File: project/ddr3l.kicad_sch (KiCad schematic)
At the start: 0 parts

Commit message: Added CubeMX project and some schematic components are added
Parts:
- added C100, C101, C102, C88, C89, C90, C91, C94, C95, C96, C97, C98, C99: 100n, bozi:GRM15_T05, symbol Device:C
- added C92, C93: 10u, bozi:GRT18_T15, symbol Device:C
- added IC9: MT41K128M16JT-107_K, bozi:BGA96C80P9X16_800X1400X120_edit, symbol bozi:MT41K128M16JT-107_K
- added R16, R17: 10K, bozi:RESC1005X37N_edit, symbol Device:R
- added R18: 100, bozi:RESC1005X37N_edit, symbol Device:R
- added R19: 240, bozi:RESC1005X37N_edit, symbol Device:R
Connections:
- new net: IC9.L8 (ZQ), R19.2
- new net DDR_A0: IC9.N3 (A0)
- new net DDR_A1: IC9.P7 (A1)
- new net DDR_A10: IC9.L7 (A10/AP)
- new net DDR_A11: IC9.R7 (A11)
- new net DDR_A12: IC9.N7 (A12/BC#)
- new net DDR_A13: IC9.T3 (A13)
- new net DDR_A2: IC9.P3 (A2)
- new net DDR_A3: IC9.N2 (A3)
- new net DDR_A4: IC9.P8 (A4)
- new net DDR_A5: IC9.P2 (A5)
- new net DDR_A6: IC9.R8 (A6)
- new net DDR_A7: IC9.R2 (A7)
- new net DDR_A8: IC9.T8 (A8)
- new net DDR_A9: IC9.R3 (A9)
- new net DDR_BA0: IC9.M2 (BA0)
- new net DDR_BA1: IC9.N8 (BA1)
- new net DDR_BA2: IC9.M3 (BA2)
- new net DDR_CKE: IC9.K9 (CKE), R17.1
- new net DDR_CLKN: IC9.K7 (CK#), R18.2
- new net DDR_CLKP: IC9.J7 (CK), R18.1
- new net DDR_DQ0: IC9.A7 (DQ12)
- new net DDR_DQ1: IC9.B8 (DQ14)
- new net DDR_DQ10: IC9.G2 (DQ6)
- new net DDR_DQ11: IC9.H8 (DQ5)
- new net DDR_DQ12: IC9.F8 (DQ3)
- new net DDR_DQ13: IC9.F2 (DQ2)
- new net DDR_DQ14: IC9.H7 (DQ7)
- new net DDR_DQ15: IC9.F7 (DQ1)
- new net DDR_DQ2: IC9.D7 (DQ8)
- new net DDR_DQ3: IC9.A3 (DQ15)
- new net DDR_DQ4: IC9.C8 (DQ10)
- new net DDR_DQ5: IC9.A2 (DQ13)
- new net DDR_DQ6: IC9.C2 (DQ11)
- new net DDR_DQ7: IC9.C3 (DQ9)
- new net DDR_DQ8: IC9.E3 (DQ0)
- new net DDR_DQ9: IC9.H3 (DQ4)
- new net DDR_DQM0: IC9.D3 (UDM)
- new net DDR_DQM1: IC9.E7 (LDM)
- new net DDR_DQS0N: IC9.B7 (UDQS#)
- new net DDR_DQS0P: IC9.C7 (UDQS)
- new net DDR_DQS1N: IC9.G3 (LDQS#)
- new net DDR_DQS1P: IC9.F3 (LDQS)
- new net DDR_ODT: IC9.K1 (ODT)
- new net GNDREF: C100.2, C101.2, C102.2, C88.2, C89.2, C90.2, C91.2, C92.2, C93.2, C94.2, C95.2, C96.2, C97.2, C98.2, C99.2, IC9.A9 (VSS_1), IC9.B1 (VSSQ_1), IC9.B3 (VSS_2), IC9.B9 (VSSQ_2), IC9.D1 (VSSQ_3), IC9.D8 (VSSQ_4), IC9.E1 (VSS_3), IC9.E2 (VSSQ_5), IC9.E8 (VSSQ_6), IC9.F9 (VSSQ_7), IC9.G1 (VSSQ_8), IC9.G8 (VSS_4), IC9.G9 (VSSQ_9), IC9.J2 (VSS_5), IC9.J8 (VSS_6), IC9.M1 (VSS_7), IC9.M9 (VSS_8), IC9.P1 (VSS_9), IC9.P9 (VSS_10), IC9.T1 (VSS_11), IC9.T9 (VSS_12), R16.2, R17.2, R19.1
- new net VDD_DDR: C100.1, C88.1, C89.1, C90.1, C91.1, C92.1, C93.1, C94.1, C95.1, C96.1, C97.1, C98.1, C99.1, IC9.A1 (VDDQ_1), IC9.A8 (VDDQ_2), IC9.B2 (VDD_1), IC9.C1 (VDDQ_3), IC9.C9 (VDDQ_4), IC9.D2 (VDDQ_5), IC9.D9 (VDD_2), IC9.E9 (VDDQ_6), IC9.F1 (VDDQ_7), IC9.G7 (VDD_3), IC9.H2 (VDDQ_8), IC9.H9 (VDDQ_9), IC9.K2 (VDD_4), IC9.K8 (VDD_5), IC9.N1 (VDD_6), IC9.N9 (VDD_7), IC9.R1 (VDD_8), IC9.R9 (VDD_9)
- new net VREF_DDR: C101.1, C102.1, IC9.H1 (VREFDQ), IC9.M8 (VREFCA)
- new net ~{DDR_CAS}: IC9.K3 (CAS#)
- new net ~{DDR_CS}: IC9.L2 (CS#)
- new net ~{DDR_RAS}: IC9.J3 (RAS#)
- new net ~{DDR_RESET}: IC9.T2 (RESET#), R16.1
- new net ~{DDR_WE}: IC9.L3 (WE#)
- no-connect marks 0 -> 5
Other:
- note added: "Connect to ground plane"

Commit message: schemtic is done, need to go through BOM
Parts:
- C100: renamed from C97; value 100n -> 100nF; Manufacturer_Name (none) -> Murata Electronics
- C101: renamed from C98; value 100n -> 100nF; Manufacturer_Name (none) -> Murata Electronics
- C102: renamed from C99; value 100n -> 100nF; Manufacturer_Name (none) -> Murata Electronics
- C103: renamed from C100; value 100n -> 100nF; Manufacturer_Name (none) -> Murata Electronics
- C104: renamed from C101; value 100n -> 100nF; Manufacturer_Name (none) -> Murata Electronics
- C105: renamed from C102; value 100n -> 100nF; Manufacturer_Name (none) -> Murata Electronics
- C91: renamed from C88; value 100n -> 100nF; Manufacturer_Name (none) -> Murata Electronics
- C92: renamed from C89; value 100n -> 100nF; Manufacturer_Name (none) -> Murata Electronics
- C93: renamed from C90; value 100n -> 100nF; Manufacturer_Name (none) -> Murata Electronics
- C94: renamed from C91; value 100n -> 100nF; Manufacturer_Name (none) -> Murata Electronics
- C95: renamed from C92; value 10u -> 10uF; Manufacturer_Name (none) -> Murata Electronics
- C96: renamed from C93; value 10u -> 10uF; Manufacturer_Name (none) -> Murata Electronics
- C97: renamed from C94; value 100n -> 100nF; Manufacturer_Name (none) -> Murata Electronics
- C98: renamed from C95; value 100n -> 100nF; Manufacturer_Name (none) -> Murata Electronics
- C99: renamed from C96; value 100n -> 100nF; Manufacturer_Name (none) -> Murata Electronics
- R20: renamed from R16; Manufacturer_Name (none) -> YAGEO
- R21: renamed from R17; Manufacturer_Name (none) -> YAGEO
- R22: renamed from R18; value 100 -> 100R; Manufacturer_Name (none) -> YAGEO
- R23: renamed from R19; value 240 -> 240R; Manufacturer_Name (none) -> YAGEO

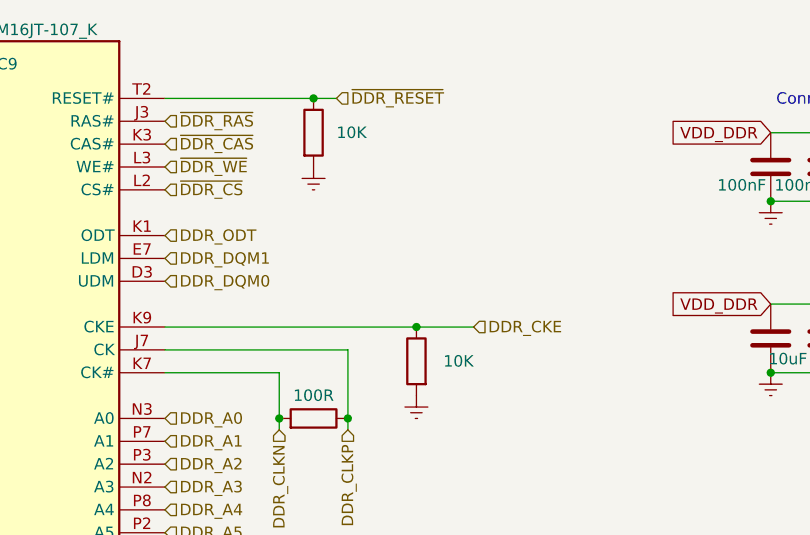
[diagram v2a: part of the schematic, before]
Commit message: schemtic is done, annotation set
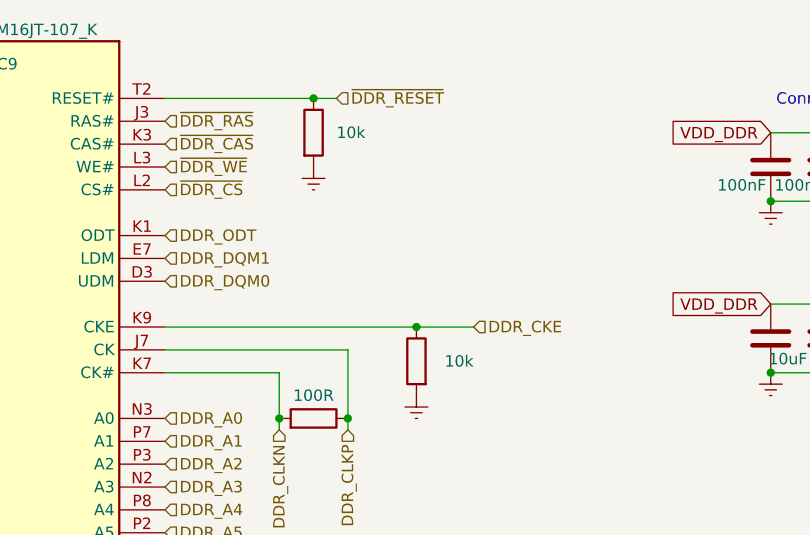
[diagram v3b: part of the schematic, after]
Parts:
- IC9: Manufacturer_Part_Number MT41K128M16JT-107:K -> MT41K128M16JT-125:K TR
- R44: renamed from R20; value 10K -> 10k
- R45: renamed from R21; value 10K -> 10k
- renumbered C97 to C100, C98 to C101, C99 to C102, C100 to C103, C101 to C104, C102 to C105, C103 to C106, C104 to C107, C105 to C108, C91 to C94, C92 to C95, C93 to C96, C94 to C97, C95 to C98, C96 to C99, R22 to R46, R23 to R47
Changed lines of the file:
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@@
 		(dnp no)
 		(fields_autoplaced yes)
-		(property "Reference" "#PWR082"
+		(property "Reference" "#PWR0102"
 			(at 214.63 68.58 0)
 			(effects
@@
 			(project "project"
 				(path "/7afeae28-8837-445b-b53a-5d89eb16eb45/bc5d602b-cd60-40f3-b6ce-866979f4c9ac"
-					(reference "#PWR082")
+					(reference "#PWR0102")
 					(unit 1)
 				)
@@
 		(dnp no)
 		(fields_autoplaced yes)
-		(property "Reference" "#PWR086"
+		(property "Reference" "#PWR0106"
 			(at 102.87 168.91 0)
 			(effects
@@
 			(project "project"
 				(path "/7afeae28-8837-445b-b53a-5d89eb16eb45/bc5d602b-cd60-40f3-b6ce-866979f4c9ac"
-					(reference "#PWR086")
+					(reference "#PWR0106")
 					(unit 1)
 				)
@@
 		(on_board yes)
 		(dnp no)
-		(property "Reference" "C95"
+		(property "Reference" "C98"
 			(at 218.44 57.1499 0)
 			(effects
@@
 			(project "project"
 				(path "/7afeae28-8837-445b-b53a-5d89eb16eb45/bc5d602b-cd60-40f3-b6ce-866979f4c9ac"
-					(reference "C95")
+					(reference "C98")
 					(unit 1)
 				)
@@
 		(dnp no)
 		(fields_autoplaced yes)
-		(property "Reference" "C91"
+		(property "Reference" "C94"
 			(at 218.44 38.0999 0)
 			(effects
@@
 			(project "project"
 				(path "/7afeae28-8837-445b-b53a-5d89eb16eb45/bc5d602b-cd60-40f3-b6ce-866979f4c9ac"
-					(reference "C91")
+					(reference "C94")
 					(unit 1)
 				)
@@
 			)
 		)
-		(property "Manufacturer_Part_Number" "MT41K128M16JT-107:K"
+		(property "Manufacturer_Part_Number" "MT41K128M16JT-125:K TR"
 			(at 109.22 635.56 0)
 			(effects
@@
 		(on_board yes)
 		(dnp no)
-		(property "Reference" "C97"
+		(property "Reference" "C100"
 			(at 231.14 57.1499 0)
 			(effects
@@
 			(project "project"
 				(path "/7afeae28-8837-445b-b53a-5d89eb16eb45/bc5d602b-cd60-40f3-b6ce-866979f4c9ac"
-					(reference "C97")
+					(reference "C100")
 					(unit 1)
 				)
@@
 		(dnp no)
 		(fields_autoplaced yes)
-		(property "Reference" "#PWR087"
+		(property "Reference" "#PWR0107"
 			(at 147.32 173.99 0)
 			(effects
@@
 			(project "project"
 				(path "/7afeae28-8837-445b-b53a-5d89eb16eb45/bc5d602b-cd60-40f3-b6ce-866979f4c9ac"
-					(reference "#PWR087")
+					(reference "#PWR0107")
 					(unit 1)
 				)
@@
 		(on_board yes)
 		(dnp no)
-		(property "Reference" "C104"
+		(property "Reference" "C107"
 			(at 86.36 90.1699 0)
 			(effects
@@
 			(project "project"
 				(path "/7afeae28-8837-445b-b53a-5d89eb16eb45/bc5d602b-cd60-40f3-b6ce-866979f4c9ac"
-					(reference "C104")
+					(reference "C107")
 					(unit 1)
 				)
@@
 		(on_board yes)
 		(dnp no)
-		(property "Reference" "C102"
+		(property "Reference" "C105"
 			(at 262.89 57.1499 0)
 			(effects
@@
 			(project "project"
 				(path "/7afeae28-8837-445b-b53a-5d89eb16eb45/bc5d602b-cd60-40f3-b6ce-866979f4c9ac"
-					(reference "C102")
+					(reference "C105")
 					(unit 1)
 				)
@@
 		(dnp no)
 		(fields_autoplaced yes)
-		(property "Reference" "#PWR084"
+		(property "Reference" "#PWR0104"
 			(at 82.55 101.6 0)
 			(effects
@@
 			(project "project"
 				(path "/7afeae28-8837-445b-b53a-5d89eb16eb45/bc5d602b-cd60-40f3-b6ce-866979f4c9ac"
-					(reference "#PWR084")
+					(reference "#PWR0104")
 					(unit 1)
 				)
@@
 		(dnp no)
 		(fields_autoplaced yes)
-		(property "Reference" "C92"
+		(property "Reference" "C95"
 			(at 224.79 38.0999 0)
 			(effects
@@
 			(project "project"
 				(path "/7afeae28-8837-445b-b53a-5d89eb16eb45/bc5d602b-cd60-40f3-b6ce-866979f4c9ac"
-					(reference "C92")
+					(reference "C95")
 					(unit 1)
 				)
@@
 		(dnp no)
 		(fields_autoplaced yes)
-		(property "Reference" "#PWR085"
+		(property "Reference" "#PWR0105"
 			(at 92.71 101.6 0)
 			(effects
@@
 			(project "project"
 				(path "/7afeae28-8837-445b-b53a-5d89eb16eb45/bc5d602b-cd60-40f3-b6ce-866979f4c9ac"
-					(reference "#PWR085")
+					(reference "#PWR0105")
 					(unit 1)
 				)
@@
 		(on_board yes)
 		(dnp no)
-		(property "Reference" "R20"
+		(property "Reference" "R44"
 			(at 166.37 34.2899 0)
 			(effects
@@
 			)
 		)
-		(property "Value" "10K"
+		(property "Value" "10k"
 			(at 166.37 35.5599 0)
 			(effects
@@
 			(project "project"
 				(path "/7afeae28-8837-445b-b53a-5d89eb16eb45/bc5d602b-cd60-40f3-b6ce-866979f4c9ac"
-					(reference "R20")
+					(reference "R44")
 					(unit 1)
 				)
@@
 		(on_board yes)
 		(dnp no)
-		(property "Reference" "C103"
+		(property "Reference" "C106"
 			(at 269.24 57.1499 0)
 			(effects
@@
 			(project "project"
 				(path "/7afeae28-8837-445b-b53a-5d89eb16eb45/bc5d602b-cd60-40f3-b6ce-866979f4c9ac"
-					(reference "C103")
+					(reference "C106")
 					(unit 1)
 				)
@@
 		(on_board yes)
 		(dnp no)
-		(property "Reference" "C96"
+		(property "Reference" "C99"
 			(at 224.79 57.1499 0)
 			(effects
@@
 			(project "project"
 				(path "/7afeae28-8837-445b-b53a-5d89eb16eb45/bc5d602b-cd60-40f3-b6ce-866979f4c9ac"
-					(reference "C96")
+					(reference "C99")
 					(unit 1)
 				)
@@
 		(on_board yes)
 		(dnp no)
-		(property "Reference" "R23"
+		(property "Reference" "R47"
 			(at 96.52 157.48 90)
 			(effects
@@
 			(project "project"
 				(path "/7afeae28-8837-445b-b53a-5d89eb16eb45/bc5d602b-cd60-40f3-b6ce-866979f4c9ac"
-					(reference "R23")
+					(reference "R47")
 					(unit 1)
 				)
@@
 		(on_board yes)
 		(dnp no)
-		(property "Reference" "C101"
+		(property "Reference" "C104"
 			(at 256.54 57.1499 0)
 			(effects
@@
 			(project "project"
 				(path "/7afeae28-8837-445b-b53a-5d89eb16eb45/bc5d602b-cd60-40f3-b6ce-866979f4c9ac"
-					(reference "C101")
+					(reference "C104")
 					(unit 1)
 				)
@@
 		(on_board yes)
 		(dnp no)
-		(property "Reference" "C100"
+		(property "Reference" "C103"
 			(at 250.19 57.1499 0)
 			(effects
@@
 			(project "project"
 				(path "/7afeae28-8837-445b-b53a-5d89eb16eb45/bc5d602b-cd60-40f3-b6ce-866979f4c9ac"
-					(reference "C100")
+					(reference "C103")
 					(unit 1)
 				)
@@
 		(on_board yes)
 		(dnp no)
-		(property "Reference" "C105"
+		(property "Reference" "C108"
 			(at 96.52 90.1699 0)
 			(effects
@@
 			(project "project"
 				(path "/7afeae28-8837-445b-b53a-5d89eb16eb45/bc5d602b-cd60-40f3-b6ce-866979f4c9ac"
-					(reference "C105")
+					(reference "C108")
 					(unit 1)
 				)
@@
 		(dnp no)
 		(fields_autoplaced yes)
-		(property "Reference" "#PWR080"
+		(property "Reference" "#PWR0100"
 			(at 163.83 45.72 0)
 			(effects
@@
 			(project "project"
 				(path "/7afeae28-8837-445b-b53a-5d89eb16eb45/bc5d602b-cd60-40f3-b6ce-866979f4c9ac"
-					(reference "#PWR080")
+					(reference "#PWR0100")
 					(unit 1)
 				)
@@
 		(on_board yes)
 		(dnp no)
-		(property "Reference" "C99"
+		(property "Reference" "C102"
 			(at 243.84 57.1499 0)
 			(effects
@@
 			(project "project"
 				(path "/7afeae28-8837-445b-b53a-5d89eb16eb45/bc5d602b-cd60-40f3-b6ce-866979f4c9ac"
-					(reference "C99")
+					(reference "C102")
 					(unit 1)
 				)
@@
 		(dnp no)
 		(fields_autoplaced yes)
-		(property "Reference" "C93"
+		(property "Reference" "C96"
 			(at 231.14 38.0999 0)
 			(effects
@@
 			(project "project"
 				(path "/7afeae28-8837-445b-b53a-5d89eb16eb45/bc5d602b-cd60-40f3-b6ce-866979f4c9ac"
-					(reference "C93")
+					(reference "C96")
 					(unit 1)
 				)
@@
 		(dnp no)
 		(fields_autoplaced yes)
-		(property "Reference" "C94"
+		(property "Reference" "C97"
 			(at 237.49 38.0999 0)
 			(effects
@@
 			(project "project"
 				(path "/7afeae28-8837-445b-b53a-5d89eb16eb45/bc5d602b-cd60-40f3-b6ce-866979f4c9ac"
-					(reference "C94")
+					(reference "C97")
 					(unit 1)
 				)
@@
 		(dnp no)
 		(fields_autoplaced yes)
-		(property "Reference" "#PWR081"
+		(property "Reference" "#PWR0101"
 			(at 214.63 49.53 0)
 			(effects
@@
 			(project "project"
 				(path "/7afeae28-8837-445b-b53a-5d89eb16eb45/bc5d602b-cd60-40f3-b6ce-866979f4c9ac"
-					(reference "#PWR081")
+					(reference "#PWR0101")
 					(unit 1)
 				)
@@
 		(on_board yes)
 		(dnp no)
-		(property "Reference" "C98"
+		(property "Reference" "C101"
 			(at 237.49 57.1499 0)
 			(effects
@@
 			(project "project"
 				(path "/7afeae28-8837-445b-b53a-5d89eb16eb45/bc5d602b-cd60-40f3-b6ce-866979f4c9ac"
-					(reference "C98")
+					(reference "C101")
 					(unit 1)
 				)
@@
 		(dnp no)
 		(fields_autoplaced yes)
-		(property "Reference" "#PWR083"
+		(property "Reference" "#PWR0103"
 			(at 175.26 71.12 0)
 			(effects
@@
 			(project "project"
 				(path "/7afeae28-8837-445b-b53a-5d89eb16eb45/bc5d602b-cd60-40f3-b6ce-866979f4c9ac"
-					(reference "#PWR083")
+					(reference "#PWR0103")
 					(unit 1)
 				)
@@
 		(on_board yes)
 		(dnp no)
-		(property "Reference" "R22"
+		(property "Reference" "R46"
 			(at 165.1001 64.77 0)
 			(effects
@@
 			(project "project"
 				(path "/7afeae28-8837-445b-b53a-5d89eb16eb45/bc5d602b-cd60-40f3-b6ce-866979f4c9ac"
-					(reference "R22")
+					(reference "R46")
 					(unit 1)
 				)
@@
 		(on_board yes)
 		(dnp no)
-		(property "Reference" "R21"
+		(property "Reference" "R45"
 			(at 172.72 59.6899 0)
 			(effects
@@
 			)
 		)
-		(property "Value" "10K"
+		(property "Value" "10k"
 			(at 181.61 60.96 0)
 			(effects
@@
 			(project "project"
 				(path "/7afeae28-8837-445b-b53a-5d89eb16eb45/bc5d602b-cd60-40f3-b6ce-866979f4c9ac"
-					(reference "R21")
+					(reference "R45")
 					(unit 1)
 				)
